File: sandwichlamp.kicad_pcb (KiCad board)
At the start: 2 copper layers, 96 x 96 mm, 27 parts, among them J1 Pole1, J2 Pole2, J3 Pole3, J4 12V Enable, J5 HLK-LD2410C, J6 Conn_01x02, J7 Conn_01x03, SW1 Rader Power, SW3 POWER, U1 magnetic-charger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

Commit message: Disconnect the two 5V nets from one another
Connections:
- U7 pad 15: +5V -> VBUS
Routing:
- net GND: track 302.5 -> 284.0 mm
- net +5V: track 98.8 -> 81.4 mm
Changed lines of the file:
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@@
 	(net 36 "unconnected-(U7-15-Pad36)")
 	(net 37 "Neopixel")
+	(net 38 "VBUS")
 	(footprint "MountingHole:MountingHole_3.2mm_M3"
 		(layer "F.Cu")
@@
 			(net 25 "unconnected-(U7-EN-Pad2)")
 			(pinfunction "EN")
-			(pintype "bidirectional")
+			(pintype "bidirectional+no_connect")
 		)
 		(pad "3" thru_hole oval
@@
 			(net 17 "unconnected-(U7-25-Pad9)")
 			(pinfunction "25")
-			(pintype "bidirectional")
+			(pintype "bidirectional+no_connect")
 		)
 		(pad "10" thru_hole oval
@@
 			(net 16 "unconnected-(U7-26-Pad10)")
 			(pinfunction "26")
-			(pintype "bidirectional")
+			(pintype "bidirectional+no_connect")
 		)
 		(pad "11" thru_hole oval
@@
 			(layers "*.Cu" "*.Mask")
 			(remove_unused_layers no)
-			(net 1 "+5V")
+			(net 38 "VBUS")
 			(pinfunction "5V")
 			(pintype "power_in")
@@
 			(net 19 "unconnected-(U7-TX-Pad18)")
 			(pinfunction "TX")
-			(pintype "output")
+			(pintype "output+no_connect")
 		)
 		(pad "19" thru_hole oval
@@
 			(net 28 "unconnected-(U7-RX-Pad19)")
 			(pinfunction "RX")
-			(pintype "input")
+			(pintype "input+no_connect")
 		)
 		(pad "20" thru_hole oval
@@
 			(net 15 "unconnected-(U7-SCL{slash}22-Pad21)")
 			(pinfunction "SCL/22")
-			(pintype "bidirectional")
+			(pintype "bidirectional+no_connect")
 		)
 		(pad "22" thru_hole oval
@@
 			(net 26 "unconnected-(U7-SCA{slash}21-Pad22)")
 			(pinfunction "SCA/21")
-			(pintype "bidirectional")
+			(pintype "bidirectional+no_connect")
 		)
 		(pad "23" thru_hole oval
@@
 			(net 29 "unconnected-(U7-17-Pad30)")
 			(pinfunction "17")
-			(pintype "bidirectional")
+			(pintype "bidirectional+no_connect")
 		)
 		(pad "31" thru_hole oval
@@
 			(net 36 "unconnected-(U7-15-Pad36)")
 			(pinfunction "15")
-			(pintype "bidirectional")
+			(pintype "bidirectional+no_connect")
 		)
 		(pad "37" thru_hole oval
@@
 	)
 	(segment
-		(start 110.6 79.6)
-		(end 100.08 79.6)
+		(start 103.030001 82.6)
+		(end 102.9 82.730001)
 		(width 1)
 		(layer "F.Cu")
@@
 	)
 	(segment
-		(start 100.08 79.6)
-		(end 100 79.68)
+		(start 110 82.6)
+		(end 103.030001 82.6)
 		(width 1)
 		(layer "F.Cu")
@@
 	)
 	(via
-		(at 100 79.68)
+		(at 102.9 82.730001)
 		(size 2)
 		(drill 0.8)
@@
 	)
 	(via
-		(at 110.6 79.6)
+		(at 110 82.6)
 		(size 2)
 		(drill 0.8)
@@
 	)
 	(segment
-		(start 100 93.457308)
-		(end 103.050001 96.507309)
+		(start 118.7 74.5)
+		(end 122.5 74.5)
 		(width 1)
 		(layer "B.Cu")
@@
 	)
 	(segment
-		(start 94.533746 100.655695)
-		(end 99.344305 100.655695)
+		(start 103.050001 98.412691)
+		(end 101.462692 100)
 		(width 1)
 		(layer "B.Cu")
@@
 	)
 	(segment
-		(start 101.462692 100)
-		(end 100 100)
+		(start 103.050001 82.880002)
+		(end 103.050001 98.412691)
 		(width 1)
 		(layer "B.Cu")
@@
 	)
 	(segment
-		(start 88.594858 68.274858)
-		(end 70.084263 68.274858)
+		(start 102.9 82.730001)
+		(end 103.050001 82.880002)
 		(width 1)
 		(layer "B.Cu")
@@
 	)
 	(segment
-		(start 113.6 79.6)
-		(end 118.7 74.5)
+		(start 110 82.6)
+		(end 110.6 82.6)
 		(width 1)
 		(layer "B.Cu")
@@
 	)
 	(segment
-		(start 100 79.68)
-		(end 88.594858 68.274858)
+		(start 110.6 82.6)
+		(end 118.7 74.5)
 		(width 1)
 		(layer "B.Cu")
@@
 	)
 	(segment
-		(start 88.2 106.989441)
-		(end 94.533746 100.655695)
+		(start 102.9 82.730001)
+		(end 102.9 82.58)
 		(width 1)
 		(layer "B.Cu")
@@
 	)
 	(segment
-		(start 99.344305 100.655695)
+		(start 101.462692 100)
 		(end 100 100)
 		(width 1)
@@
 	)
 	(segment
-		(start 103.050001 96.507309)
-		(end 103.050001 98.412691)
-		(width 1)
-		(layer "B.Cu")
-		(net 1)
-	)
-	(segment
-		(start 118.7 74.5)
-		(end 122.5 74.5)
-		(width 1)
-		(layer "B.Cu")
-		(net 1)
-	)
-	(segment
-		(start 100 79.68)
-		(end 100 93.457308)
-		(width 1)
-		(layer "B.Cu")
-		(net 1)
-	)
-	(segment
-		(start 110.6 79.6)
-		(end 113.6 79.6)
-		(width 1)
-		(layer "B.Cu")
-		(net 1)
-	)
-	(segment
-		(start 103.050001 98.412691)
-		(end 101.462692 100)
+		(start 88.594858 68.274858)
+		(end 70.084263 68.274858)
 		(width 1)
 		(layer "B.Cu")
@@
 	)
 	(segment
-		(start 88.2 108.14)
-		(end 88.2 106.989441)
+		(start 102.9 82.58)
+		(end 88.594858 68.274858)
 		(width 1)
 		(layer "B.Cu")
@@
 	)
 	(segment
-		(start 90.099441 102.55)
-		(end 99.999999 102.55)
-		(width 1)
-		(layer "F.Cu")
-		(net 2)
-	)
-	(segment
-		(start 85.66 106.989441)
-		(end 90.099441 102.55)
-		(width 1)
-		(layer "F.Cu")
-		(net 2)
-	)
-	(segment
 		(start 108.52 132.474416)
 		(end 109.845584 133.8)
@@
 	)
 	(segment
-		(start 85.66 108.14)
-		(end 85.66 106.989441)
-		(width 1)
-		(layer "F.Cu")
-		(net 2)
-	)
-	(segment
 		(start 108.52 131)
 		(end 108.52 132.474416)
@@
 	)
 	(segment
+		(start 66.662943 67.587057)
+		(end 66.662943 68.813336)
+		(width 1)
+		(layer "B.Cu")
+		(net 2)
+	)
+	(segment
 		(start 140.403792 100.894497)
 		(end 138.283774 100.894497)
@@
 	)
 	(segment
-		(start 85.66 106.983857)
-		(end 85.66 108.14)
-		(width 1)
-		(layer "B.Cu")
-		(net 2)
-	)
-	(segment
 		(start 130.806445 102.958676)
 		(end 128.738507 102.958676)
@@
 	)
 	(segment
-		(start 95.5 91)
-		(end 95.5 97.143857)
+		(start 74.680457 63.395821)
+		(end 70.854179 63.395821)
 		(width 1)
 		(layer "B.Cu")
@@
 	)
 	(segment
-		(start 95.45 79.95)
-		(end 95.45 90.95)
-		(width 1)
-		(layer "B.Cu")
-		(net 2)
-	)
-	(segment
 		(start 142.267351 115.4875)
 		(end 143.875685 113.879166)
@@
 	)
 	(segment
-		(start 74.680457 63.395821)
-		(end 70.854179 63.395821)
-		(width 1)
-		(layer "B.Cu")
-		(net 2)
-	)
-	(segment
 		(start 133.02 100.745121)
 		(end 130.806445 102.958676)
@@
 	)
 	(segment
-		(start 95.5 89.792443)
-		(end 95.5 91)
-		(width 1)
-		(layer "B.Cu")
-		(net 2)
-	)
-	(segment
-		(start 95.45 90.95)
-		(end 95.5 91)
+		(start 66.662943 68.813336)
+		(end 74.049608 76.200001)
 		(width 1)
 		(layer "B.Cu")
@@
 	)
 	(segment
-		(start 66.662943 67.587057)
-		(end 66.662943 68.813336)
-		(width 1)
-		(layer "B.Cu")
-		(net 2)
-	)
-	(segment
 		(start 122.36 96.580169)
 		(end 122.36 94.6)
@@
 	)
 	(segment
-		(start 70.854179 63.395821)
-		(end 66.662943 67.587057)
-		(width 1)
-		(layer "B.Cu")
-		(net 2)
-	)
-	(segment
 		(start 127.962861 81.767435)
 		(end 127.962861 90.950251)
@@
 	)
 	(segment
-		(start 91.700001 76.200001)
-		(end 95.45 79.95)
-		(width 1)
-		(layer "B.Cu")
-		(net 2)
-	)
-	(segment
-		(start 74.049608 76.200001)
-		(end 91.700001 76.200001)
-		(width 1)
-		(layer "B.Cu")
-		(net 2)
-	)
-	(segment
-		(start 95.5 97.143857)
-		(end 85.66 106.983857)
+		(start 136.713926 111.45)
+		(end 128.100357 111.45)
 		(width 1)
 		(layer "B.Cu")
@@
 	)
 	(segment
-		(start 136.713926 111.45)
-		(end 128.100357 111.45)
+		(start 95.6 80.1)
+		(end 95.6 97.043857)
 		(width 1)
 		(layer "B.Cu")
@@
 	)
 	(segment
-		(start 66.662943 68.813336)
-		(end 74.049608 76.200001)
-		(width 1)
-		(layer "B.Cu")
-		(net 2)
-	)
-	(segment
 		(start 143.875685 106.875685)
 		(end 141.288241 106.875685)
@@
 	)
 	(segment
+		(start 95.6 97.043857)
+		(end 85.66 106.983857)
+		(width 1)
+		(layer "B.Cu")
+		(net 2)
+	)
+	(segment
 		(start 119.415076 118.334924)
 		(end 131.457244 118.334924)
@@
 	)
 	(segment
+		(start 74.049608 76.200001)
+		(end 91.700001 76.200001)
+		(width 1)
+		(layer "B.Cu")
+		(net 2)
+	)
+	(segment
 		(start 81 109.150458)
 		(end 81 97.009686)
@@
 	)
 	(segment
+		(start 91.700001 76.200001)
+		(end 95.6 80.1)
+		(width 1)
+		(layer "B.Cu")
+		(net 2)
+	)
+	(segment
 		(start 136.972392 111.191534)
 		(end 136.713926 111.45)
 		(width 1)
 		(layer "B.Cu")
+		(net 2)
+	)
+	(segment
+		(start 85.66 106.983857)
+		(end 85.66 108.14)
+		(width 1)
+		(layer "B.Cu")
+		(net 2)
+	)
+	(segment
+		(start 70.854179 63.395821)
+		(end 66.662943 67.587057)
+		(width 1)
+		(layer "B.Cu")

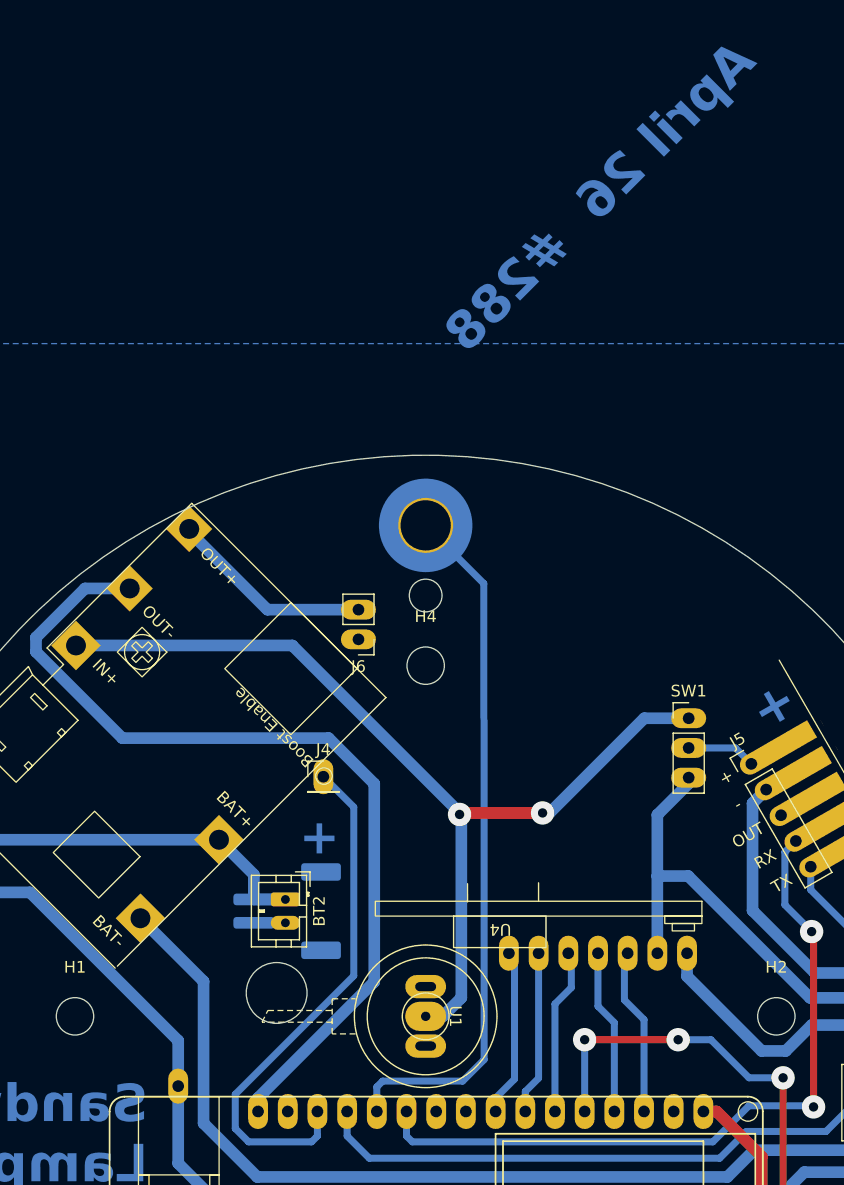
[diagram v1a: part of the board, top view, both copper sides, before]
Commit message: Relocate the logo
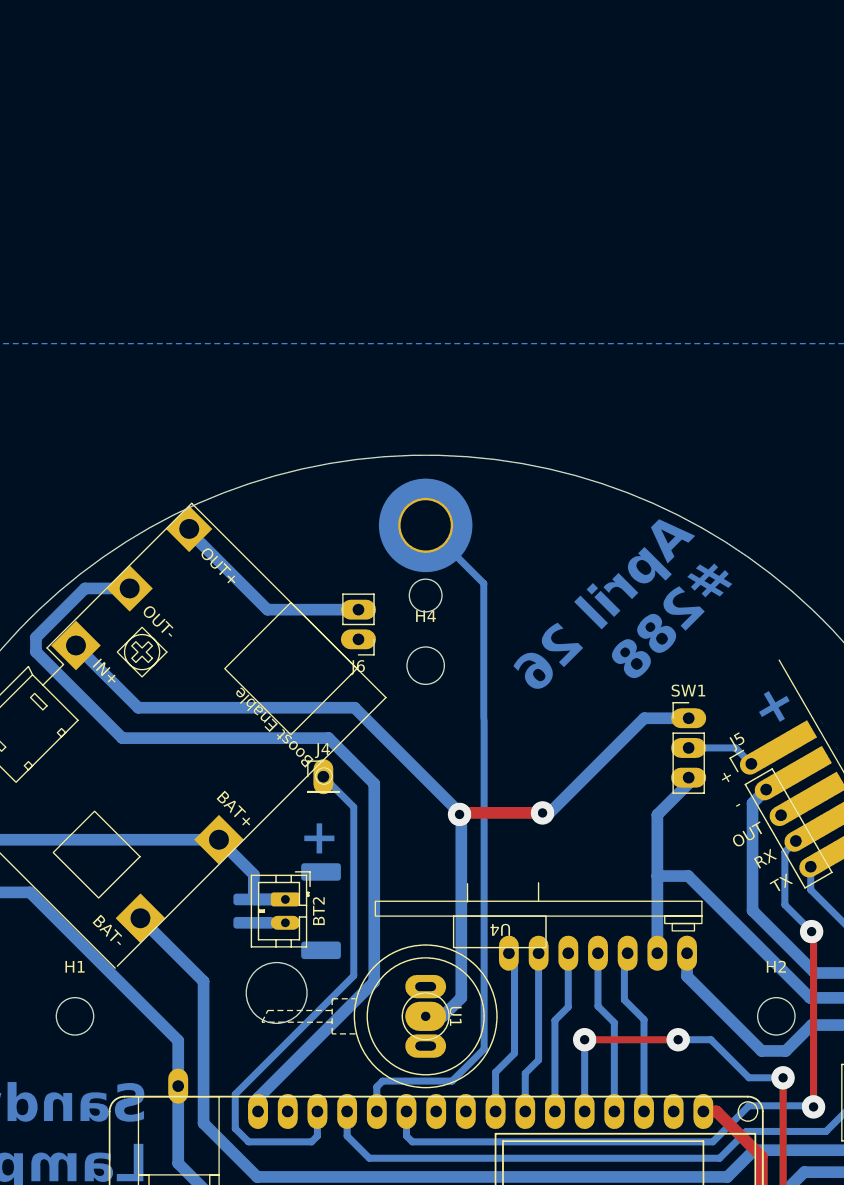
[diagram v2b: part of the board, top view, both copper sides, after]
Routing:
- net Touch1: track 59.8 -> 59.3 mm
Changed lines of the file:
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@@
 		(layer "Edge.Cuts")
 	)
-	(gr_text "April 26  #288"
-		(at 128.682804 18.72 45)
+	(gr_text "April 26\n#288"
+		(at 127 62.8 45)
 		(layer "B.Cu" knockout)
 		(effects
@@
 	)
 	(segment
+		(start 102.9 82.730001)
+		(end 102.9 82.58)
+		(width 1)
+		(layer "B.Cu")
+		(net 1)
+	)
+	(segment
 		(start 118.7 74.5)
 		(end 122.5 74.5)
@@
 	)
 	(segment
+		(start 75.409405 73.6)
+		(end 70.084263 68.274858)
+		(width 1)
+		(layer "B.Cu")
+		(net 1)
+	)
+	(segment
 		(start 103.050001 82.880002)
 		(end 103.050001 98.412691)
@@
 	)
 	(segment
-		(start 102.9 82.730001)
-		(end 102.9 82.58)
+		(start 102.9 82.58)
+		(end 93.92 73.6)
 		(width 1)
 		(layer "B.Cu")
@@
 	)
 	(segment
-		(start 88.594858 68.274858)
-		(end 70.084263 68.274858)
-		(width 1)
-		(layer "B.Cu")
-		(net 1)
-	)
-	(segment
-		(start 102.9 82.58)
-		(end 88.594858 68.274858)
+		(start 93.92 73.6)
+		(end 75.409405 73.6)
 		(width 1)
 		(layer "B.Cu")
@@
 	)
 	(segment
-		(start 108.52 106.429747)
+		(start 109.66 94.6)
+		(end 109.66 103.74)
+		(width 0.6)
+		(layer "B.Cu")
+		(net 10)
+	)
+	(segment
+		(start 108.52 104.88)
 		(end 108.52 108.14)
 		(width 0.6)
@@
 	)
 	(segment
-		(start 109.66 94.6)
-		(end 109.66 105.289747)
-		(width 0.6)
-		(layer "B.Cu")
-		(net 10)
-	)
-	(segment
-		(start 109.66 105.289747)
-		(end 108.52 106.429747)
+		(start 109.66 103.74)
+		(end 108.52 104.88)
 		(width 0.6)
 		(layer "B.Cu")
@@
 	)
 	(segment
-		(start 112.46 94.86)
-		(end 112.46 97.54)
+		(start 112.2 94.6)
+		(end 112.2 99.2)
 		(width 0.6)
 		(layer "B.Cu")
@@
 	)
 	(segment
-		(start 112.2 94.6)
-		(end 112.46 94.86)
+		(start 111.06 100.34)
+		(end 111.06 108.14)
 		(width 0.6)
 		(layer "B.Cu")
@@
 	)
 	(segment
-		(start 112.46 97.54)
-		(end 111.06 98.94)
-		(width 0.6)
-		(layer "B.Cu")
-		(net 12)
-	)
-	(segment
-		(start 111.06 98.94)
-		(end 111.06 108.14)
+		(start 112.2 99.2)
+		(end 111.06 100.34)
 		(width 0.6)
 		(layer "B.Cu")
@@
 	)
 	(segment
-		(start 105 103.705)
-		(end 103.165 105.54)
+		(start 105 74.68)
+		(end 105 102.8)
 		(width 0.6)
 		(layer "B.Cu")
@@
 	)
 	(segment
-		(start 105 74.68)
-		(end 105 103.705)
+		(start 105 102.8)
+		(end 102.26 105.54)
 		(width 0.6)
 		(layer "B.Cu")
@@
 	)
 	(segment
-		(start 103.165 105.54)
+		(start 102.26 105.54)
 		(end 96.32 105.54)
 		(width 0.6)
@@
 	)
 	(segment
-		(start 105.98 106.989849)
-		(end 105.98 108.14)
-		(width 0.6)
-		(layer "B.Cu")
-		(net 27)
-	)
-	(segment
-		(start 107.6 95.08)
-		(end 107.6 105.369849)
-		(width 0.6)
-		(layer "B.Cu")
-		(net 27)
-	)
-	(segment
 		(start 107.12 94.6)
 		(end 107.6 95.08)
@@
 	)
 	(segment
-		(start 107.6 105.369849)
-		(end 105.98 106.989849)
-		(width 0.6)
-		(layer "B.Cu")
+		(start 105.98 104.789171)
+		(end 105.98 108.14)
+		(width 0.6)
+		(layer "B.Cu")
+		(net 27)
+	)
+	(segment
+		(start 107.6 103.169171)
+		(end 105.98 104.789171)
+		(width 0.6)
+		(layer "B.Cu")
+		(net 27)
+	)
+	(segment
+		(start 107.6 95.08)
+		(end 107.6 103.169171)
+		(width 0.6)
+		(layer "B.Cu")

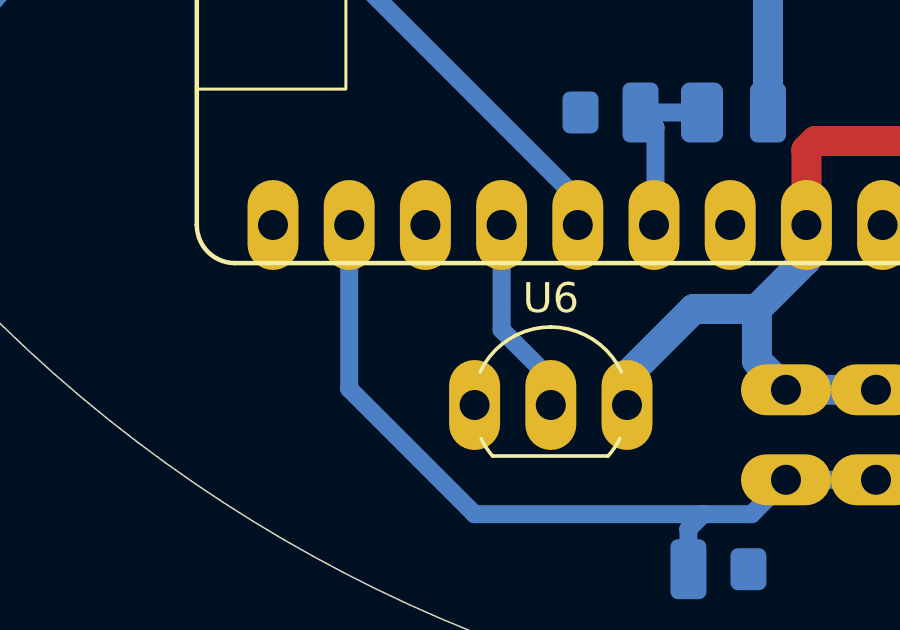
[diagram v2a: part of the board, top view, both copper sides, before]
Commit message: Thicker GND trace for the temperature sensor
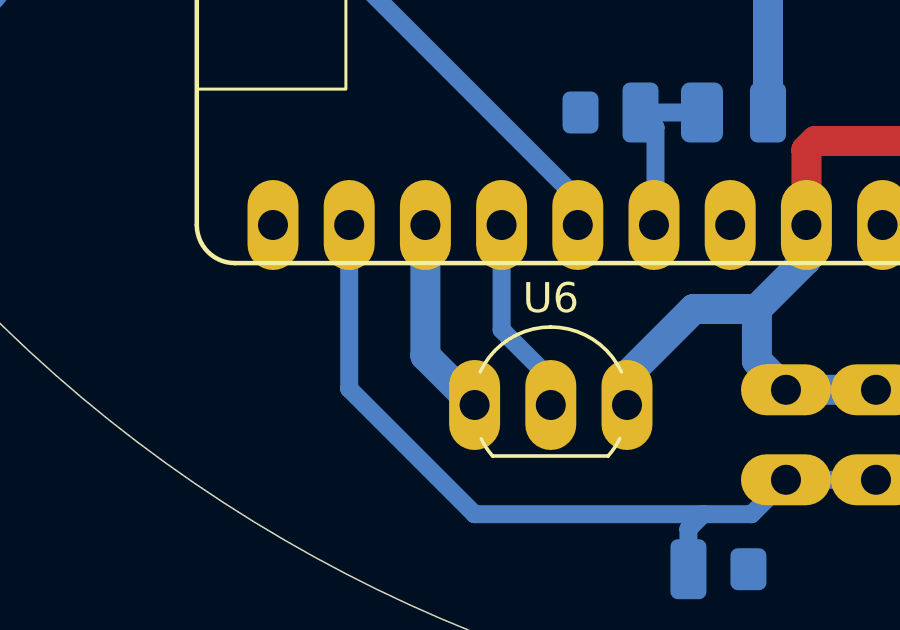
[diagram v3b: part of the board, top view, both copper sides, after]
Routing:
- net GND: track 284.0 -> 290.7 mm
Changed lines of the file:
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@@
+	)
+	(segment
+		(start 82.22 137)
+		(end 80.58 135.36)
+		(width 1)
+		(layer "B.Cu")
+		(net 2)
 	)
 	(segment
@@
 		(width 1)
 		(layer "B.Cu")
+		(net 2)
+	)
+	(segment
+		(start 80.58 135.36)
+		(end 80.58 131)
+		(width 1)
+		(layer "B.Cu")
